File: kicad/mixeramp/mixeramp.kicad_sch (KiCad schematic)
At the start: 23 parts, among them Q1 NPN, Q2 NPN, U1 ${SIM.PARAMS}

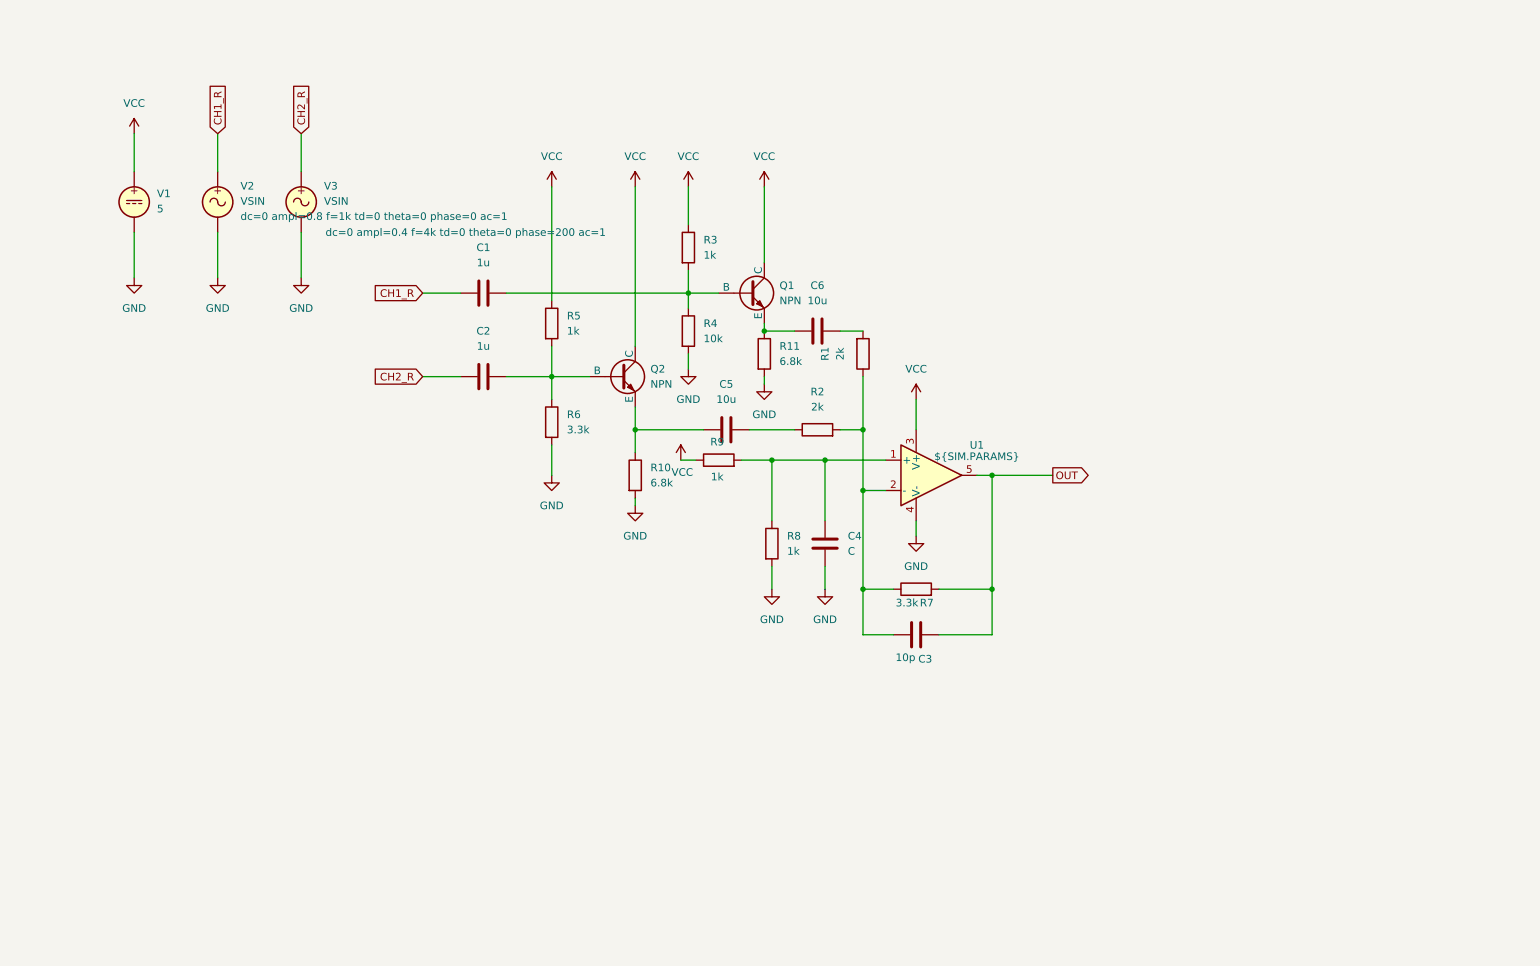
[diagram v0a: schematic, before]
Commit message: remove buffer
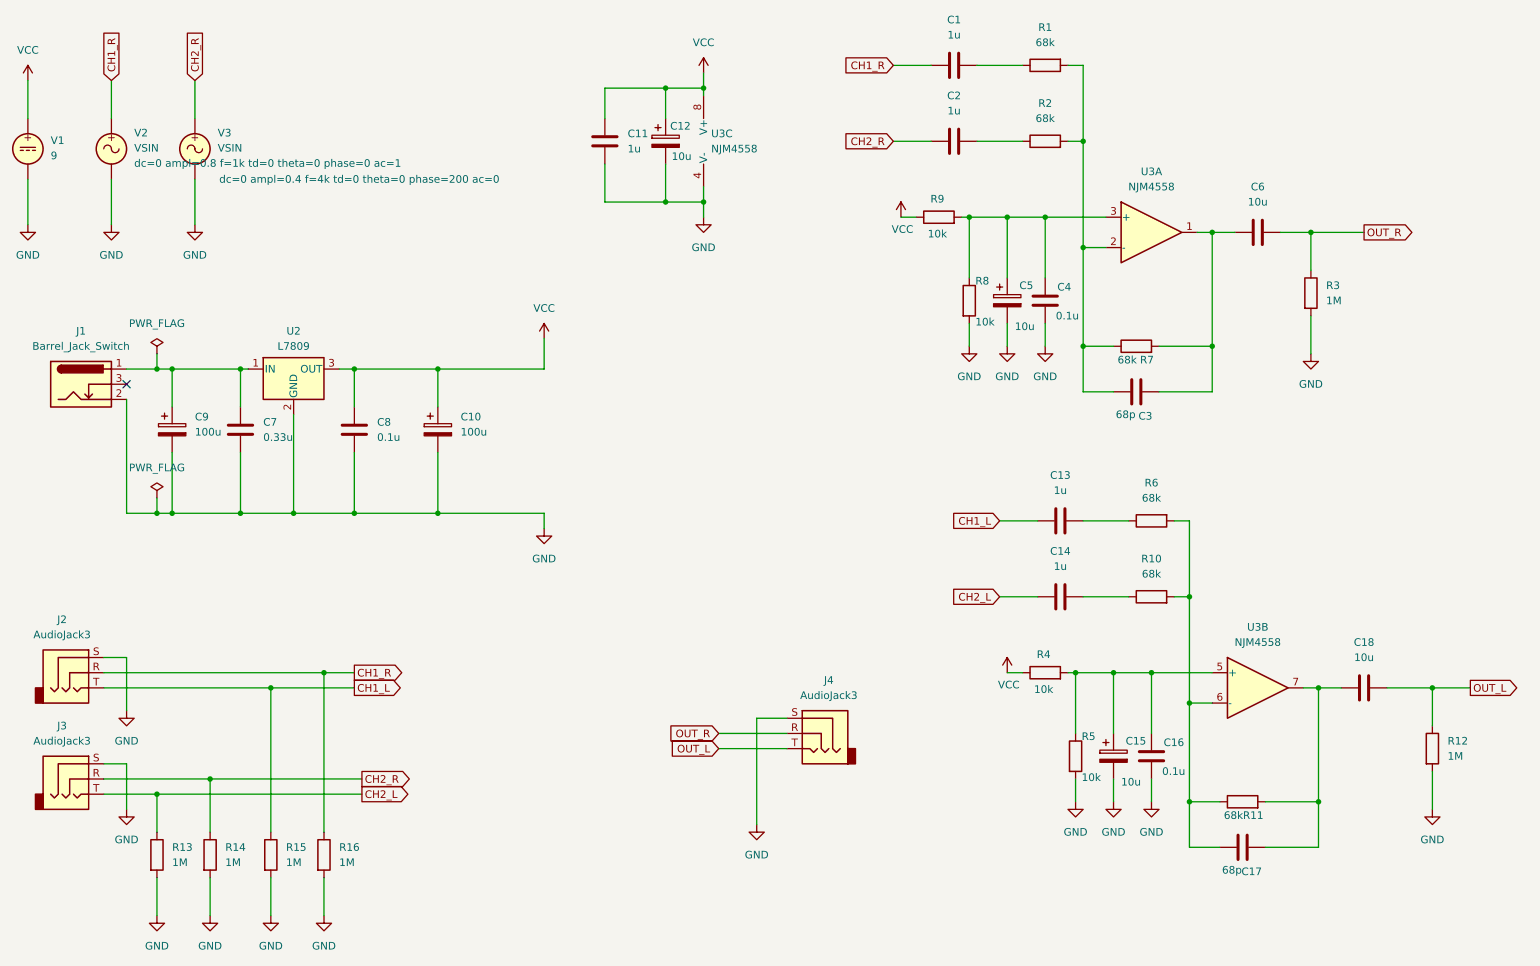
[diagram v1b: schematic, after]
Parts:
- removed C5: 10u, symbol Device:C
- removed Q1, Q2: NPN, symbol Simulation_SPICE:NPN
- removed U1: ${SIM.PARAMS}, symbol Simulation_SPICE:OPAMP
- added C10, C9: 100u, symbol Device:C_Polarized
- added C11, C13, C14: 1u, symbol Device:C
- added C12, C15, C5: 10u, symbol Device:C_Polarized
- added C16, C8: 0.1u, symbol Device:C
- added C17: 68p, symbol Device:C
- added C18: 10u, symbol Device:C
- added C7: 0.33u, symbol Device:C
- added J1: Barrel_Jack_Switch, symbol Connector:Barrel_Jack_Switch
- added J2, J3, J4: AudioJack3, symbol Connector_Audio:AudioJack3
- added R12, R13, R14, R15, R16: 1M, symbol Device:R
- added U2: L7809, symbol Regulator_Linear:L7809
- added U3: NJM4558, symbol Amplifier_Operational:NJM4558
- C3: value 10p -> 68p
- C4: value C -> 0.1u
- R1, R2: value 2k -> 68k
- R10, R11: value 6.8k -> 68k
- R3: value 1k -> 1M
- R5, R8, R9: value 1k -> 10k
- R6, R7: value 3.3k -> 68k
- V1: value 5 -> 9; now left out of the parts list
- V2, V3: now left out of the parts list
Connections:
- net OUT is gone; now on an unnamed net: C3.2, R7.2
- net CH1_R: now also J2.R, R16.1
- net CH2_R: now also J3.R, R14.1
- net GND: now also R3.2, R5.2, C10.2, C11.2, C12.2, C15.2, C16.2, C5.2, C7.2, C8.2, C9.2, J1.2, J2.S, J3.S, J4.S, R12.2, R13.2, R14.2, R15.2, R16.2, U2.2 (GND), U3.4 (V-); no longer R10.2, R11.2, R4.2, R6.2
- net VCC: now also R4.1, C10.1, C11.1, C12.1, C8.1, U2.3 (OUT), U3.8 (V+); no longer R3.1, R5.1
- net at C4.1, R8.1, R9.2: now also C5.1, U3.3 (+)
- net at R10.1: now also C14.2
- net at R2.1: now also C2.2
- net at C3.1, R2.2, R7.1: now also R1.2, U3.2 (-); no longer R1.1
- net at C6.1: now also U3.1; no longer R11.1
- net OUT_R: now reaches C6.2
- net OUT_R: now also R3.1, J4.R; no longer R1.2
- new net: C1.2, R1.1
- new net: C7.1, C9.1, J1.1, U2.1 (IN)
- new net: C15.1, C16.1, R4.2, R5.1, U3.5 (+)
- new net: C17.2, C18.1, R11.2, U3.7
- new net: C17.1, R10.2, R11.1, R6.2, U3.6 (-)
- new net: C13.2, R6.1
- new net CH1_L: C13.1, J2.T, R15.1
- new net CH2_L: C14.1, J3.T, R13.1
- new net OUT_L: C18.2, J4.T, R12.1
- no-connect marks 0 -> 1
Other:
- moved on the sheet: C3, C4, R1, R2, R7, R8, R9, V1, V2, V3

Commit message: wip: making BOM and footprint list
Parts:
- C11, C16, C17, C3, C4, C8: footprint (none) -> Capacitor_THT:C_Disc_D3.8mm_W2.6mm_P2.50mm
- C7: footprint (none) -> Capacitor_THT:C_Disc_D3.8mm_W2.6mm_P2.50mm; MPN (none) -> RD15W334K1HL2L; URL (none) -> https://akizukidenshi.com/catalog/g/g115937/
- J1: footprint (none) -> Connector_BarrelJack:BarrelJack_Horizontal
- J2, J3, J4: footprint (none) -> Connector_Audio:Jack_3.5mm_Switronic_ST-005-G_horizontal; MPN (none) -> ST-005-G; URL (none) -> https://akizukidenshi.com/catalog/g/g102460/
- R1, R10, R12, R13, R14, R15, R16, R2, R3, R4, R5, R6, R8, R9: footprint (none) -> Resistor_THT:R_Axial_DIN0411_L9.9mm_D3.6mm_P15.24mm_Horizontal
- R11, R7: footprint (none) -> Resistor_THT:R_Axial_DIN0204_L3.6mm_D1.6mm_P2.54mm_Vertical
- U3: footprint (none) -> Package_DIP:DIP-8_W7.62mm

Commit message: make BOM and footprint list
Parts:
- C1, C13, C14, C2: value 1u -> 100u; footprint (none) -> Capacitor_THT:CP_Radial_D8.0mm_P3.50mm; URL (none) -> https://akizukidenshi.com/catalog/g/g105041/
- C10, C9: footprint (none) -> Capacitor_THT:CP_Radial_D5.0mm_P2.50mm
- C12, C15, C5, C6: footprint (none) -> Capacitor_THT:C_Disc_D3.8mm_W2.6mm_P2.50mm; MPN (none) -> RD20F106Z1EH5L; URL (none) -> https://akizukidenshi.com/catalog/g/g103095/; purchase (none) -> 1
- C17, C3: value 68p -> 3p
- C18: value 10u -> 100u; footprint (none) -> Capacitor_THT:CP_Radial_D8.0mm_P3.50mm; URL (none) -> https://akizukidenshi.com/catalog/g/g105041/
- C7: purchase (none) -> 1
- J1: purchase (none) -> 0
- J2, J3, J4: purchase (none) -> 3
- R1, R10, R11, R2, R6, R7: URL (none) -> https://akizukidenshi.com/catalog/g/g107852/; purchase (none) -> 6
- R12, R13, R14, R15, R16, R3: URL (none) -> https://akizukidenshi.com/catalog/g/g125105/; purchase (none) -> 6
- R8, R9: value 10k -> 1k
- U2: footprint (none) -> Package_TO_SOT_THT:TO-220-3_Vertical; MPN (none) -> L7809CV; URL (none) -> https://akizukidenshi.com/catalog/g/g111165/; purchase (none) -> 1
- U3: value NJM4558 -> NJM4580; purchase (none) -> 0
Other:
- note added: "Optional"

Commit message: place footprints
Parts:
- added H1, H2, H3, H4: MountingHole, MountingHole:MountingHole_3.2mm_M3, symbol Mechanical:MountingHole
- C6: value 10u -> 100u; footprint Capacitor_THT:C_Disc_D3.8mm_W2.6mm_P2.50mm -> Capacitor_THT:CP_Radial_D8.0mm_P3.50mm; MPN RD20F106Z1EH5L -> (none); URL https://akizukidenshi.com/catalog/g/g103095/ -> https://akizukidenshi.com/catalog/g/g105041/

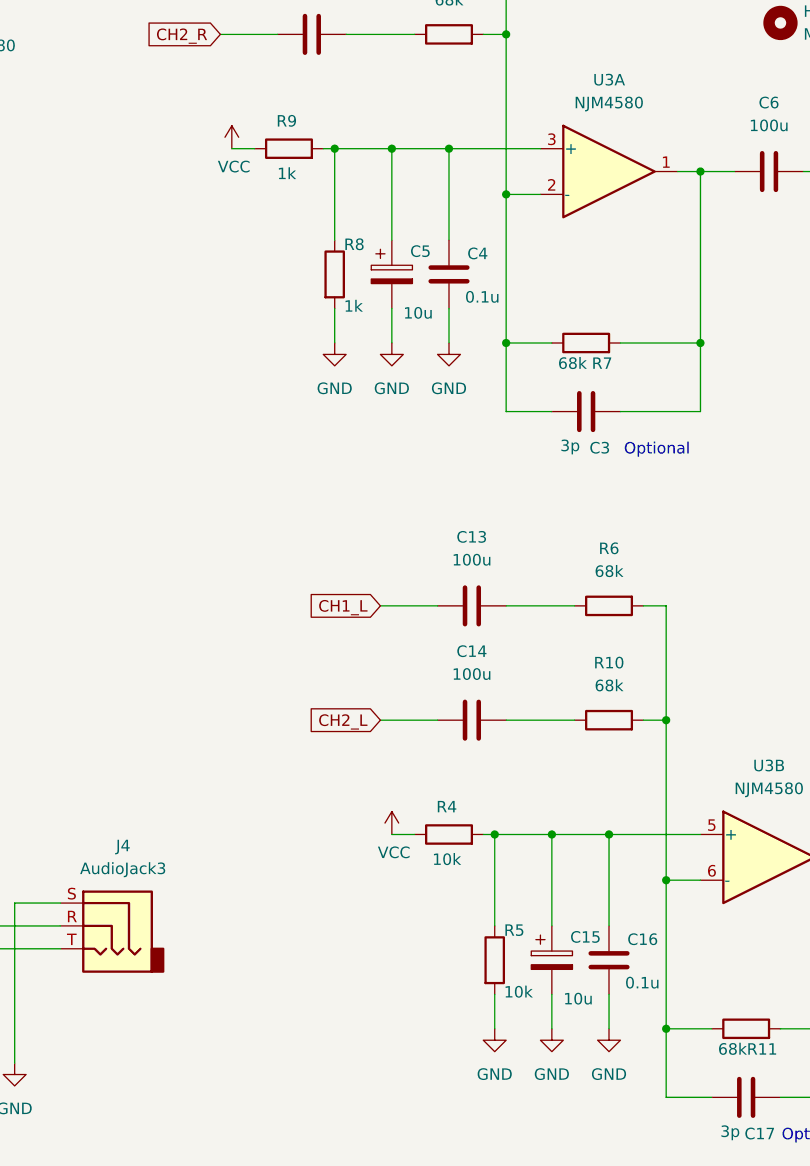
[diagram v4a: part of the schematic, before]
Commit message: add MPNs for several components
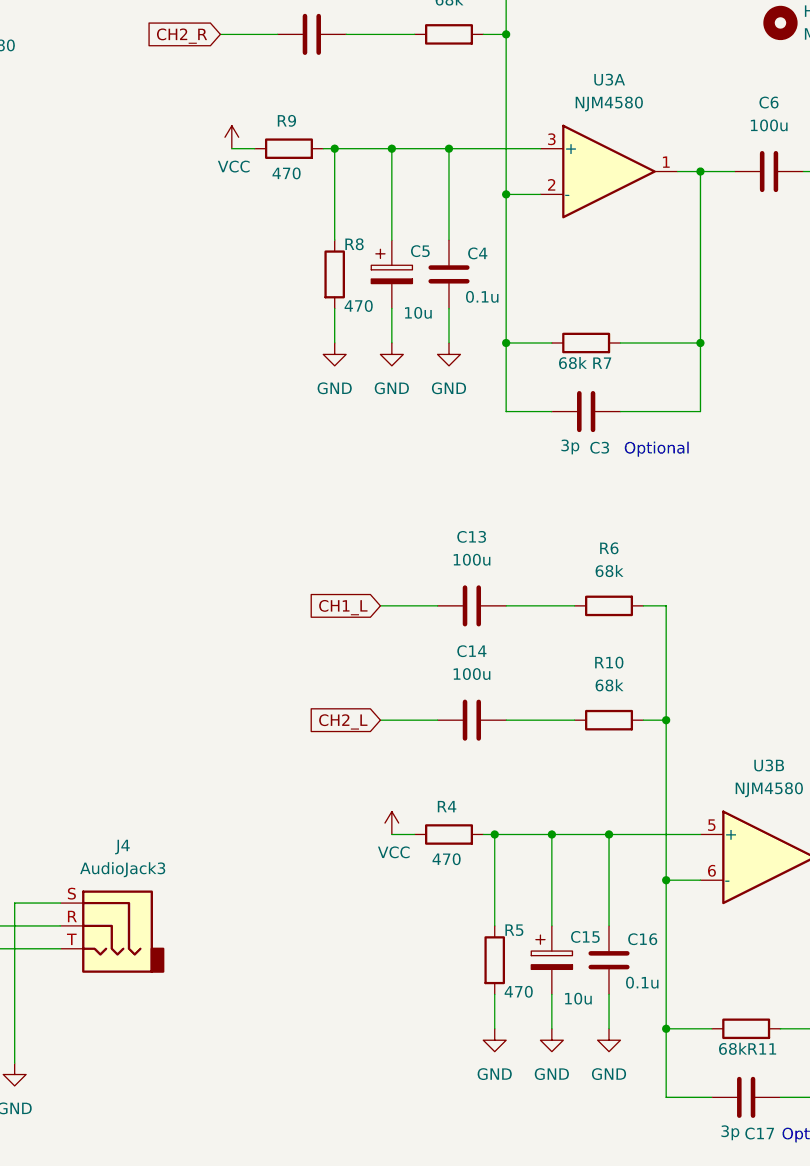
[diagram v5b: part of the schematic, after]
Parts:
- C10, C11, C16, C17, C3, C4, C8, C9, H1, H2, H3, H4: purchase (none) -> 0
- R1, R10, R11, R2, R6, R7: URL https://akizukidenshi.com/catalog/g/g107852/ -> https://akizukidenshi.com/catalog/g/g108562/; note (none) -> buy 47kOhm and several values at the same time.
- R4, R5: value 10k -> 470; URL (none) -> https://akizukidenshi.com/catalog/g/g108532/; purchase (none) -> 1
- R8, R9: value 1k -> 470; URL (none) -> https://akizukidenshi.com/catalog/g/g108532/; purchase (none) -> 1
